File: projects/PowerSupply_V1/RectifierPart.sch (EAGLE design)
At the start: 17 parts, among them X1 IN, X2 PRI, X3 SEC

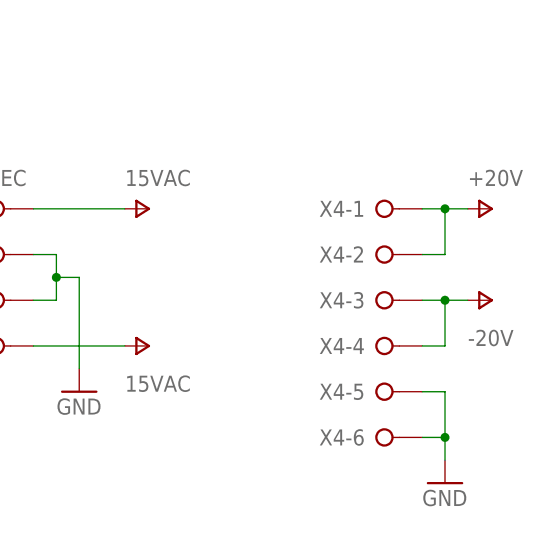
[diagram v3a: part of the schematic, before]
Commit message: feat(rectifier): schematics and routing changed
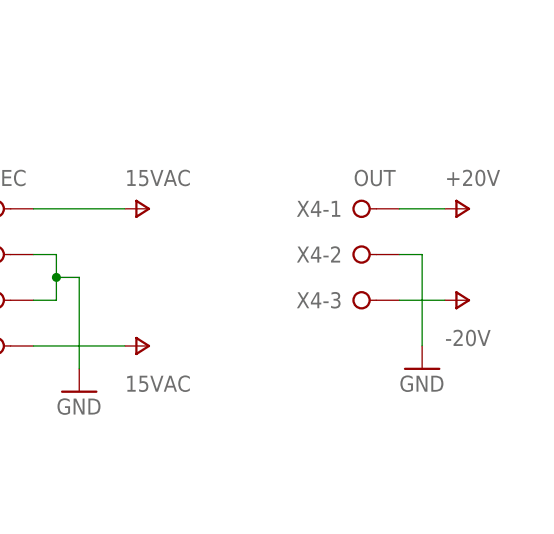
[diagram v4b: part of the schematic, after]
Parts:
- C5, C6: device rcl:CPOL-EUE5-13 -> rcl:CPOL-EUE7.5-16
- X4: value (none) -> OUT; device con-wago-508:W237-06P -> con-wago-508:W237-03P
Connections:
- net GND: now also X4-2.KL; no longer X4-5.KL, X4-6.KL
- net V+: no longer X4-2.KL
- net V-: no longer X4-4.KL
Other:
- moved on the sheet: X4-1, X4-2, X4-3
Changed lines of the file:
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@@
 <layer number="18" name="Vias" color="2" fill="1" visible="no" active="no"/>
 <layer number="19" name="Unrouted" color="6" fill="1" visible="no" active="no"/>
-<layer number="20" name="Dimension" color="15" fill="1" visible="no" active="no"/>
+<layer number="20" name="Dimension" color="24" fill="1" visible="no" active="no"/>
 <layer number="21" name="tPlace" color="7" fill="1" visible="no" active="no"/>
 <layer number="22" name="bPlace" color="7" fill="1" visible="no" active="no"/>
@@
 <part name="C3" library="rcl" library_urn="urn:adsk.eagle:library:334" deviceset="C-EU" device="050-024X044" package3d_urn="urn:adsk.eagle:package:23643/1" value="10nF"/>
 <part name="C4" library="rcl" library_urn="urn:adsk.eagle:library:334" deviceset="C-EU" device="050-024X044" package3d_urn="urn:adsk.eagle:package:23643/1" value="10nF"/>
-<part name="C5" library="rcl" library_urn="urn:adsk.eagle:library:334" deviceset="CPOL-EU" device="E5-13" package3d_urn="urn:adsk.eagle:package:23375/1" value="2200µF"/>
-<part name="C6" library="rcl" library_urn="urn:adsk.eagle:library:334" deviceset="CPOL-EU" device="E5-13" package3d_urn="urn:adsk.eagle:package:23375/1" value="2200µF"/>
+<part name="C5" library="rcl" library_urn="urn:adsk.eagle:library:334" deviceset="CPOL-EU" device="E7.5-16" package3d_urn="urn:adsk.eagle:package:23382/2" value="2200µF"/>
+<part name="C6" library="rcl" library_urn="urn:adsk.eagle:library:334" deviceset="CPOL-EU" device="E7.5-16" package3d_urn="urn:adsk.eagle:package:23382/2" value="2200µF"/>
 <part name="FRAME1" library="frames" library_urn="urn:adsk.eagle:library:229" deviceset="A4L-LOC" device=""/>
 <part name="R1" library="varistor" library_urn="urn:adsk.eagle:library:410" deviceset="S20K275" device="" package3d_urn="urn:adsk.eagle:package:30604/1"/>
@@
 <part name="P+4" library="supply1" library_urn="urn:adsk.eagle:library:371" deviceset="V+" device="" value="15VAC"/>
 <part name="P-4" library="supply1" library_urn="urn:adsk.eagle:library:371" deviceset="V-" device="" value="15VAC"/>
-<part name="X4" library="con-wago-508" library_urn="urn:adsk.eagle:library:196" deviceset="W237-06P" device="" package3d_urn="urn:adsk.eagle:package:10742/1"/>
 <part name="P+5" library="supply1" library_urn="urn:adsk.eagle:library:371" deviceset="V+" device="" value="+20V"/>
 <part name="P-5" library="supply1" library_urn="urn:adsk.eagle:library:371" deviceset="V-" device="" value="-20V"/>
@@
 <part name="P-6" library="supply1" library_urn="urn:adsk.eagle:library:371" deviceset="V-" device="" value="-20V"/>
 <part name="GND1" library="supply1" library_urn="urn:adsk.eagle:library:371" deviceset="GND" device=""/>
+<part name="X4" library="con-wago-508" library_urn="urn:adsk.eagle:library:196" deviceset="W237-03P" device="" package3d_urn="urn:adsk.eagle:package:10737/1" value="OUT"/>
 </parts>
 <sheets>
@@
 <attribute name="VALUE" x="20.32" y="101.6" size="1.778" layer="96" rot="MR0"/>
 </instance>
-<instance part="X4" gate="-1" x="137.16" y="40.64" smashed="yes">
-<attribute name="NAME" x="135.89" y="41.529" size="1.778" layer="95" rot="R180"/>
-</instance>
-<instance part="X4" gate="-2" x="137.16" y="35.56" smashed="yes">
-<attribute name="NAME" x="135.89" y="36.449" size="1.778" layer="95" rot="R180"/>
-</instance>
-<instance part="X4" gate="-3" x="137.16" y="30.48" smashed="yes">
-<attribute name="NAME" x="135.89" y="31.369" size="1.778" layer="95" rot="R180"/>
-</instance>
-<instance part="X4" gate="-4" x="137.16" y="25.4" smashed="yes">
-<attribute name="NAME" x="135.89" y="26.289" size="1.778" layer="95" rot="R180"/>
-</instance>
-<instance part="X4" gate="-5" x="137.16" y="20.32" smashed="yes">
-<attribute name="NAME" x="135.89" y="21.209" size="1.778" layer="95" rot="R180"/>
-</instance>
-<instance part="X4" gate="-6" x="137.16" y="15.24" smashed="yes">
-<attribute name="VALUE" x="137.16" y="17.78" size="1.778" layer="96"/>
-<attribute name="NAME" x="135.89" y="16.129" size="1.778" layer="95" rot="R180"/>
-</instance>
-<instance part="P+5" gate="1" x="149.86" y="40.64" smashed="yes" rot="R270">
-<attribute name="VALUE" x="147.32" y="43.18" size="1.778" layer="96"/>
-</instance>
-<instance part="P-5" gate="1" x="149.86" y="30.48" smashed="yes" rot="R90">
-<attribute name="VALUE" x="147.32" y="25.4" size="1.778" layer="96"/>
-</instance>
-<instance part="GND5" gate="1" x="144.78" y="10.16" smashed="yes">
-<attribute name="VALUE" x="142.24" y="7.62" size="1.778" layer="96"/>
+<instance part="P+5" gate="1" x="147.32" y="40.64" smashed="yes" rot="R270">
+<attribute name="VALUE" x="144.78" y="43.18" size="1.778" layer="96"/>
+</instance>
+<instance part="P-5" gate="1" x="147.32" y="30.48" smashed="yes" rot="R90">
+<attribute name="VALUE" x="144.78" y="25.4" size="1.778" layer="96"/>
+</instance>
+<instance part="GND5" gate="1" x="142.24" y="22.86" smashed="yes">
+<attribute name="VALUE" x="139.7" y="20.32" size="1.778" layer="96"/>
 </instance>
 <instance part="P+6" gate="1" x="73.66" y="127" smashed="yes" rot="R270">
@@
 <instance part="GND1" gate="1" x="73.66" y="109.22" smashed="yes" rot="R90">
 <attribute name="VALUE" x="76.2" y="106.68" size="1.778" layer="96" rot="R90"/>
+</instance>
+<instance part="X4" gate="-1" x="134.62" y="40.64" smashed="yes">
+<attribute name="NAME" x="133.35" y="41.529" size="1.778" layer="95" rot="R180"/>
+</instance>
+<instance part="X4" gate="-2" x="134.62" y="35.56" smashed="yes">
+<attribute name="NAME" x="133.35" y="36.449" size="1.778" layer="95" rot="R180"/>
+</instance>
+<instance part="X4" gate="-3" x="134.62" y="30.48" smashed="yes">
+<attribute name="VALUE" x="134.62" y="43.18" size="1.778" layer="96"/>
+<attribute name="NAME" x="133.35" y="31.369" size="1.778" layer="95" rot="R180"/>
 </instance>
 </instances>
@@
 </segment>
 <segment>
-<pinref part="X4" gate="-5" pin="KL"/>
-<wire x1="142.24" y1="20.32" x2="144.78" y2="20.32" width="0.1524" layer="91"/>
-<pinref part="GND5" gate="1" pin="GND"/>
-<wire x1="144.78" y1="20.32" x2="144.78" y2="15.24" width="0.1524" layer="91"/>
-<pinref part="X4" gate="-6" pin="KL"/>
-<wire x1="144.78" y1="15.24" x2="144.78" y2="12.7" width="0.1524" layer="91"/>
-<wire x1="142.24" y1="15.24" x2="144.78" y2="15.24" width="0.1524" layer="91"/>
-<junction x="144.78" y="15.24"/>
-</segment>
-<segment>
 <pinref part="C6" gate="G$1" pin="+"/>
 <wire x1="66.04" y1="101.6" x2="66.04" y2="109.22" width="0.1524" layer="91"/>
@@
 <junction x="66.04" y="109.22"/>
 </segment>
+<segment>
+<pinref part="X4" gate="-2" pin="KL"/>
+<wire x1="139.7" y1="35.56" x2="142.24" y2="35.56" width="0.1524" layer="91"/>
+<pinref part="GND5" gate="1" pin="GND"/>
+<wire x1="142.24" y1="35.56" x2="142.24" y2="25.4" width="0.1524" layer="91"/>
+</segment>
 </net>
 <net name="PE" class="0">
@@
 <wire x1="22.86" y1="111.76" x2="20.32" y2="111.76" width="0.1524" layer="91"/>
 <pinref part="P+4" gate="1" pin="V+"/>
-</segment>
-<segment>
-<pinref part="X4" gate="-1" pin="KL"/>
-<pinref part="P+5" gate="1" pin="V+"/>
-<wire x1="142.24" y1="40.64" x2="144.78" y2="40.64" width="0.1524" layer="91"/>
-<pinref part="X4" gate="-2" pin="KL"/>
-<wire x1="144.78" y1="40.64" x2="147.32" y2="40.64" width="0.1524" layer="91"/>
-<wire x1="142.24" y1="35.56" x2="144.78" y2="35.56" width="0.1524" layer="91"/>
-<wire x1="144.78" y1="35.56" x2="144.78" y2="40.64" width="0.1524" layer="91"/>
-<junction x="144.78" y="40.64"/>
 </segment>
 <segment>
@@
 <junction x="66.04" y="127"/>
 </segment>
+<segment>
+<pinref part="P+5" gate="1" pin="V+"/>
+<pinref part="X4" gate="-1" pin="KL"/>
+<wire x1="144.78" y1="40.64" x2="139.7" y2="40.64" width="0.1524" layer="91"/>
+</segment>
 </net>
 <net name="V-" class="0">
@@
 <wire x1="55.88" y1="104.14" x2="50.8" y2="104.14" width="0.1524" layer="91"/>
 <junction x="50.8" y="104.14"/>
-</segment>
-<segment>
-<pinref part="P-5" gate="1" pin="V-"/>
-<pinref part="X4" gate="-3" pin="KL"/>
-<wire x1="147.32" y1="30.48" x2="144.78" y2="30.48" width="0.1524" layer="91"/>
-<pinref part="X4" gate="-4" pin="KL"/>
-<wire x1="144.78" y1="30.48" x2="142.24" y2="30.48" width="0.1524" layer="91"/>
-<wire x1="142.24" y1="25.4" x2="144.78" y2="25.4" width="0.1524" layer="91"/>
-<wire x1="144.78" y1="25.4" x2="144.78" y2="30.48" width="0.1524" layer="91"/>
-<junction x="144.78" y="30.48"/>
 </segment>
 <segment>
@@
 <junction x="66.04" y="91.44"/>
 </segment>
+<segment>
+<pinref part="P-5" gate="1" pin="V-"/>
+<pinref part="X4" gate="-3" pin="KL"/>
+<wire x1="144.78" y1="30.48" x2="139.7" y2="30.48" width="0.1524" layer="91"/>
+</segment>
 </net>

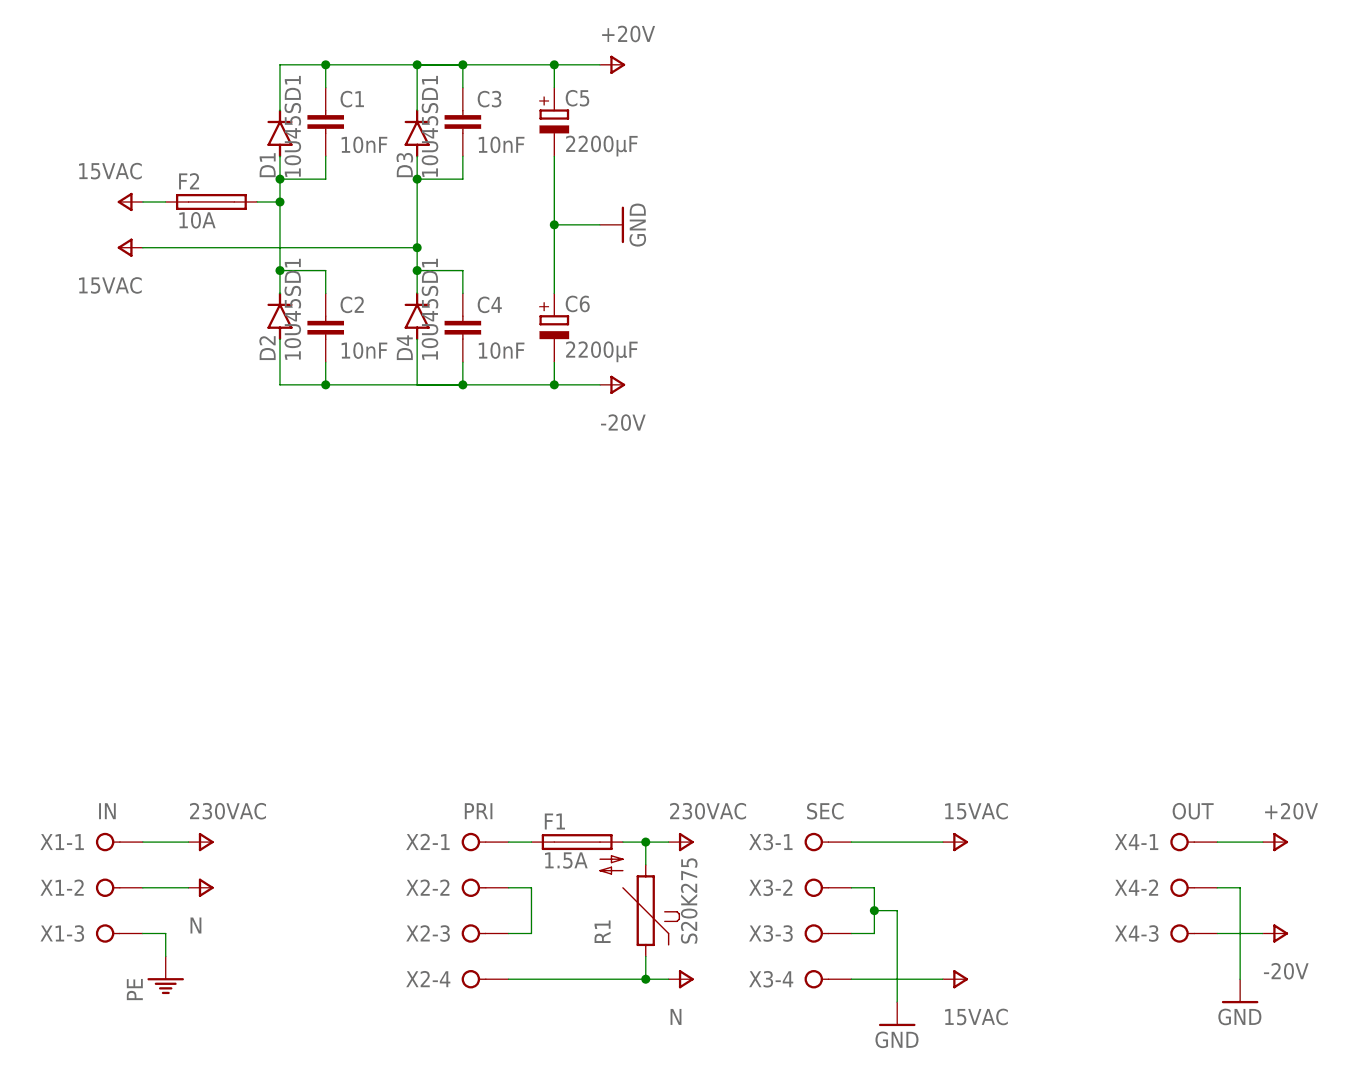
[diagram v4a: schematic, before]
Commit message: feat: rectifier power sources modified
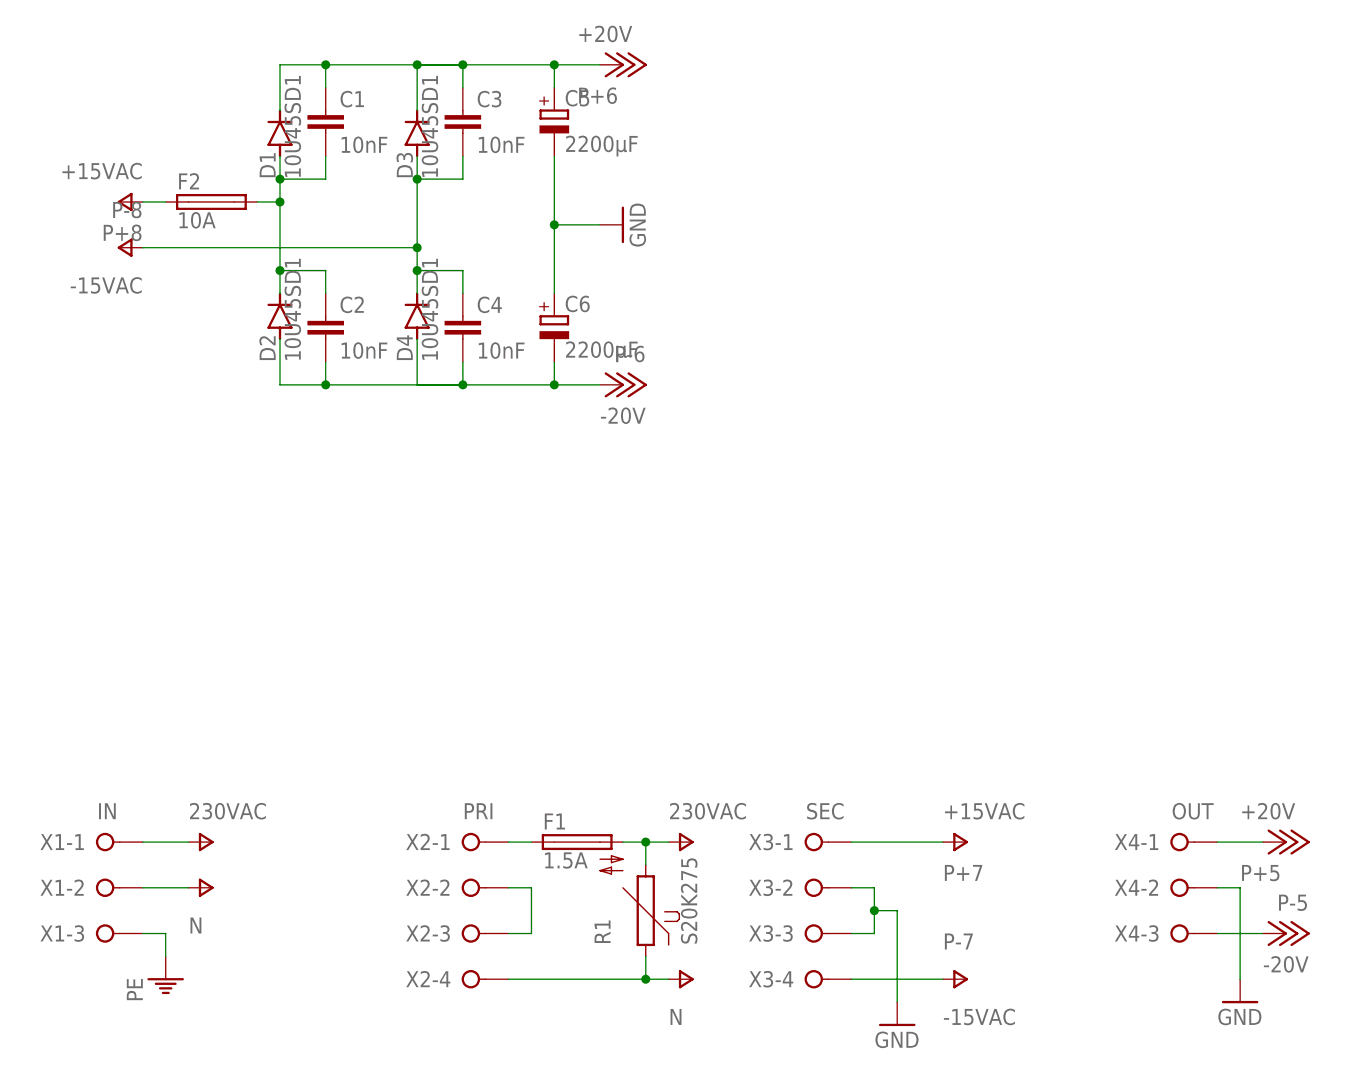
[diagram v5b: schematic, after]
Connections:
- new net +15VAC: F2.1, X3-1.KL
- new net +20V: C1.1, C3.1, C5.+, D1.C, D3.C, X4-1.KL
- new net -15VAC: C3.2, C4.1, D3.A, D4.C, X3-4.KL
- new net -20V: C2.2, C4.2, C6.-, D2.A, D4.A, X4-3.KL
- net V+: no longer C1.1, C3.1, C5.+, D1.C, D3.C, F2.1, X3-1.KL, X4-1.KL
- net V-: no longer C2.2, C3.2, C4.1, C4.2, C6.-, D2.A, D3.A, D4.A, D4.C, X3-4.KL, X4-3.KL
